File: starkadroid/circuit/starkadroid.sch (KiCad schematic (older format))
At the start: 19 parts, among them IC1 ATMEGA8-P, X1 16MHz

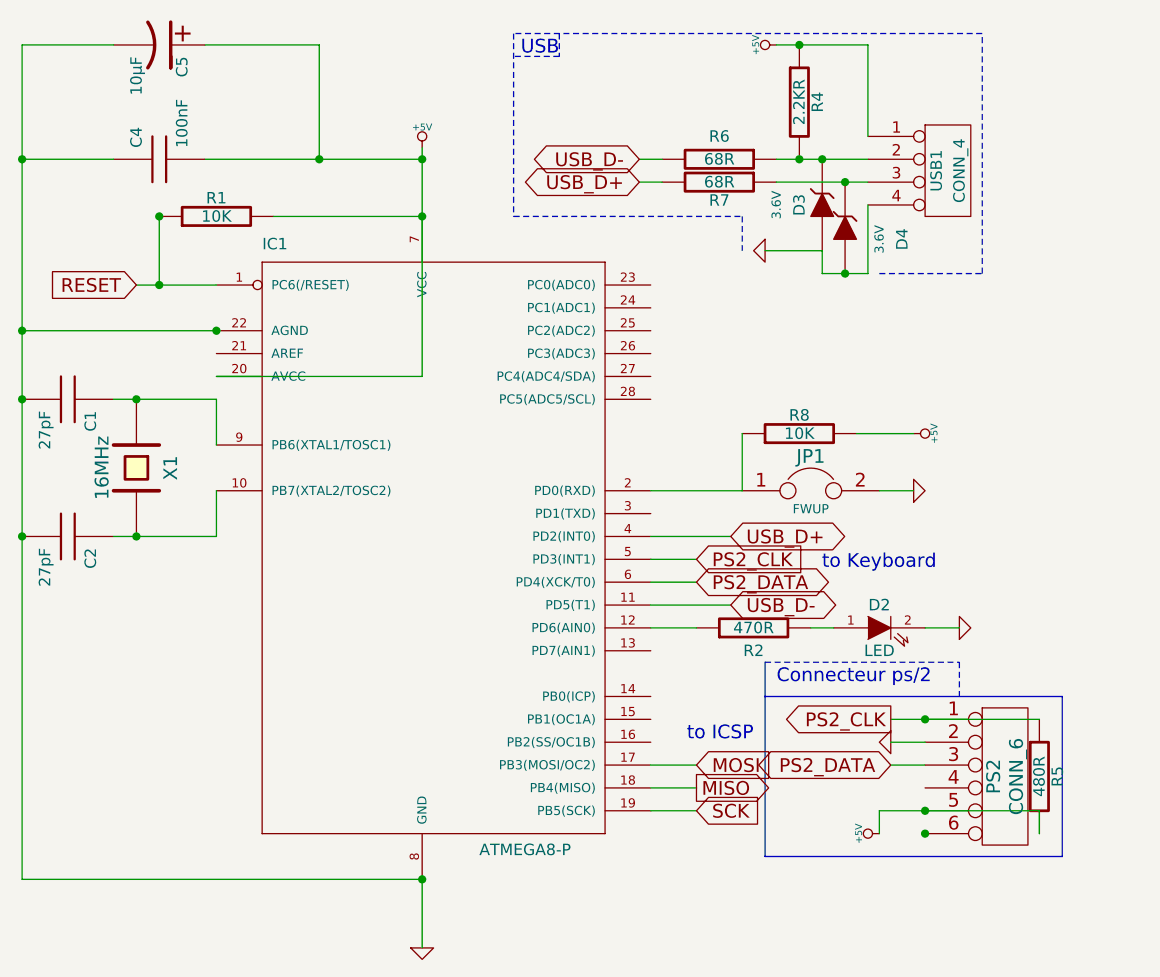
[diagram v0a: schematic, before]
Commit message: Circuit finalisé prêt à être réalisé.
git-svn-id: svn://pulkomandy.tk/avrstuff@24 c6672c3c-f6b6-47f9-9001-1fd6b12fecbe
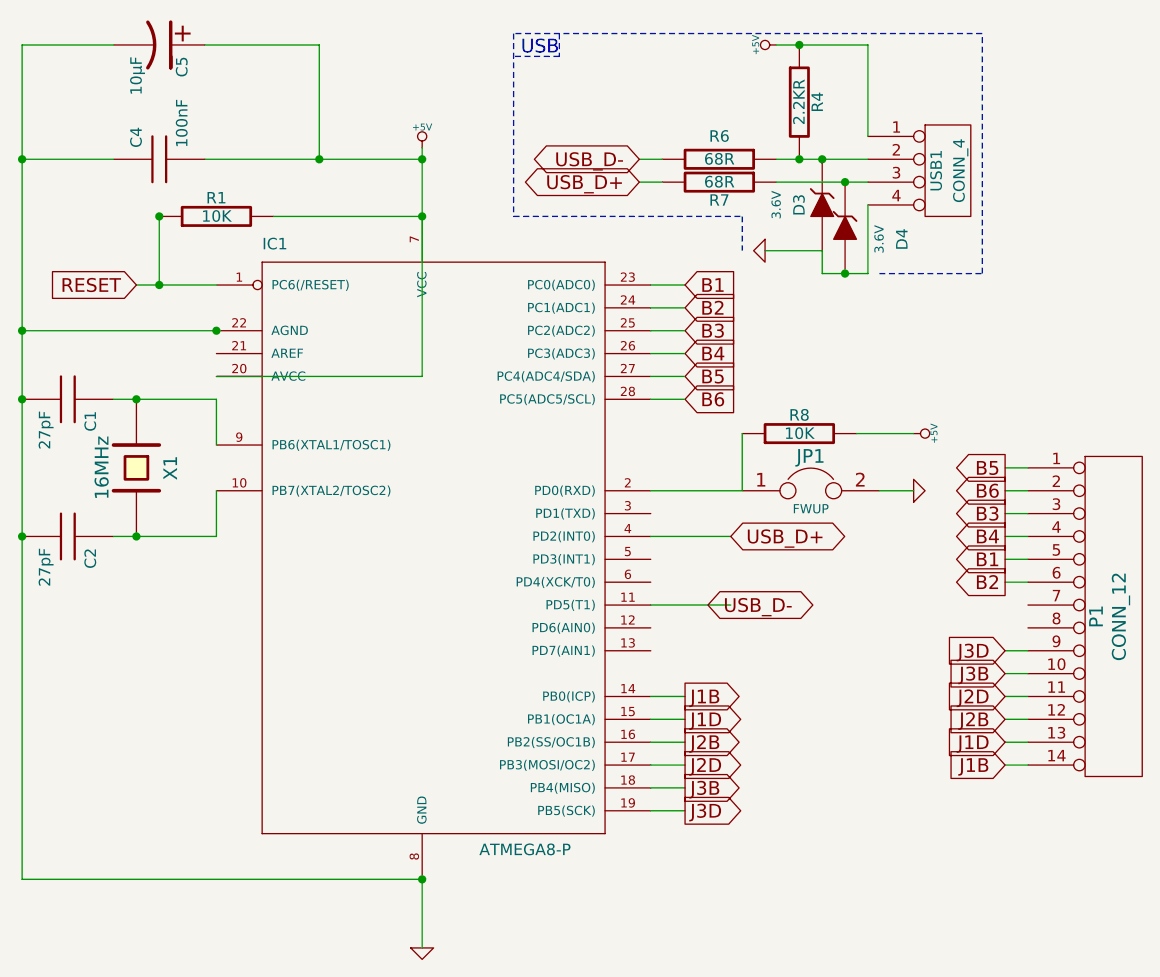
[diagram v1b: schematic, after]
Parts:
- removed D2: LED, symbol LED
- removed PS2: CONN_6, Mini_din6, symbol CONN_6
- removed R2: 470R, symbol R
- removed R5: 480R, symbol R
- added P1: CONN_12, CONN_14, symbol CONN_14
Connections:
- net J1B: now reaches IC1.14 (PB0(ICP))
- net J1B: now also P1.14 (P14)
- net J1D: now reaches IC1.15 (PB1(OC1A))
- net J1D: now also P1.13 (P13)
- net J2B: now reaches IC1.16 (PB2(SS/OC1B))
- net J2B: now also P1.12 (P12)
- net B1: now reaches IC1.23 (PC0(ADC0))
- net B1: now also P1.5 (P5)
- net B2: now reaches IC1.24 (PC1(ADC1))
- net B2: now also P1.6 (P6)
- net B3: now reaches IC1.25 (PC2(ADC2))
- net B3: now also P1.3 (P3)
- net B4: now reaches IC1.26 (PC3(ADC3))
- net B4: now also P1.4 (P4)
- net B5: now reaches IC1.27 (PC4(ADC4/SDA))
- net B5: now also P1.1 (P1)
- net B6: now reaches IC1.28 (PC5(ADC5/SCL))
- net B6: now also P1.2 (P2)
- net MISO renamed J3B
- net J3B: now also P1.10 (P10)
- net MOSI renamed J2D
- net J2D: now also P1.11 (P11)
- net PS2_CLK: no longer names the net of IC1.5 (PD3(INT1))
- net PS2_DATA: no longer names the net of IC1.6 (PD4(XCK/T0))
- net SCK renamed J3D
- net J3D: now also P1.9 (P9)
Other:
- note removed: "Connecteur ps/2"
- note removed: "to ICSP"
- note removed: "to Keyboard"
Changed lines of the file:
@@
-EESchema Schematic File Version 2  date 30/08/2010 19:46:30
+EESchema Schematic File Version 2  date 16/10/2010 15:14:04
 LIBS:power
 LIBS:device
@@
 LIBS:contrib
 LIBS:valves
-LIBS:ps2toserial-cache
+LIBS:starkadroid-cache
 EELAYER 24  0
 EELAYER END
 $Descr User 6000 6000
 Sheet 1 1
-Title "PS/2 to serial converter"
-Date "30 aug 2010"
-Rev "2010.06.22"
+Title "Starkadroid USB Arcade buttons device"
+Date "16 oct 2010"
+Rev "2010.10.16"
 Comp "PulkoTronics"
 Comment1 ""
@@
 Comment4 ""
 $EndDescr
-Connection ~ 4550 4000
-Wire Wire Line
-	5050 4100 5050 4000
-Wire Wire Line
-	5050 4000 4350 4000
+Wire Wire Line
+	4900 3800 5000 3800
+Wire Wire Line
+	4900 3700 5000 3700
+Wire Wire Line
+	4900 3600 5000 3600
+Wire Wire Line
+	4900 3500 5000 3500
+Wire Wire Line
+	4900 3400 5000 3400
+Wire Wire Line
+	4900 3300 5000 3300
+Wire Wire Line
+	3350 4000 3500 4000
+Wire Wire Line
+	3350 3800 3500 3800
+Wire Wire Line
+	3350 3600 3500 3600
+Wire Wire Line
+	4900 2500 5000 2500
+Wire Wire Line
+	4900 2700 5000 2700
+Wire Wire Line
+	4900 3000 5000 3000
+Wire Wire Line
+	3350 2200 3500 2200
+Wire Wire Line
+	3350 2000 3500 2000
+Wire Wire Line
+	3350 1800 3500 1800
 Wire Wire Line
 	4500 2350 4250 2350
 Wire Wire Line
 	3750 2350 3750 2600
-Wire Bus Line
-	3850 3500 5150 3500
-Wire Bus Line
-	5150 3500 5150 4200
-Wire Bus Line
-	5150 4200 3850 4200
-Wire Bus Line
-	3850 4200 3850 3350
-Wire Wire Line
-	4400 3600 5050 3600
-Wire Wire Line
-	1000 650  600  650
+Wire Wire Line
+	600  650  1000 650
 Wire Wire Line
 	600  650  600  4300
-Wire Wire Line
-	4550 3800 4400 3800
 Wire Wire Line
 	3700 3100 3350 3100
@@
 Connection ~ 4200 1650
 Wire Wire Line
-	4300 1350 4300 1650
+	4300 1650 4300 1350
 Wire Wire Line
 	4300 1650 4100 1650
@@
 	3300 1150 3400 1150
 Wire Wire Line
-	4300 1050 4300 650
+	4300 650  4300 1050
 Connection ~ 4100 1150
 Connection ~ 600  1150
@@
 	600  1150 1000 1150
 Wire Wire Line
-	4050 3200 4150 3200
-Wire Wire Line
-	1700 1400 2350 1400
+	2350 1400 1700 1400
 Connection ~ 600  1900
 Wire Wire Line
 	1100 1700 1450 1700
-Wire Wire Line
-	3350 4000 3550 4000
-Wire Wire Line
-	3350 3800 3550 3800
 Wire Wire Line
 	600  1900 1450 1900
@@
 	1000 2200 1450 2200
 Wire Wire Line
-	1450 2600 1450 2800
+	1450 2800 1450 2600
 Connection ~ 2350 4300
-Wire Notes Line
-	3850 3350 4700 3350
-Wire Wire Line
-	3350 2900 3550 2900
-Wire Wire Line
-	3350 3000 3550 3000
-Wire Notes Line
-	4700 3350 4700 3500
-Wire Wire Line
-	1450 2100 2350 2100
-Wire Wire Line
-	2350 2100 2350 1100
+Wire Wire Line
+	2350 2100 1450 2100
+Wire Wire Line
+	2350 1100 2350 2100
 Connection ~ 2350 1400
 Wire Wire Line
 	1450 2200 1450 2400
 Wire Wire Line
-	1450 2800 1000 2800
+	1000 2800 1450 2800
 Connection ~ 1100 2800
 Connection ~ 1450 1900
@@
 	2350 4300 600  4300
 Connection ~ 600  2800
-Wire Wire Line
-	3350 3900 3550 3900
 Connection ~ 1200 1700
 Connection ~ 2350 1150
 Connection ~ 1200 1400
 Wire Wire Line
-	3350 3200 3550 3200
-Wire Wire Line
-	4550 3200 4700 3200
-Wire Wire Line
 	1400 1150 2350 1150
 Connection ~ 1900 1150
@@
 Connection ~ 4200 1250
 Wire Wire Line
-	4300 650  3900 650
+	3900 650  4300 650
 Connection ~ 4000 650
 Wire Wire Line
@@
 	3700 2800 3350 2800
 Wire Wire Line
-	4550 3700 4400 3700
-Wire Wire Line
 	1200 1400 1200 1700
 Wire Wire Line
@@
 Wire Wire Line
 	1900 650  1900 1150
-Connection ~ 4550 3600
-Connection ~ 4550 4100
 Wire Wire Line
 	3750 2600 3350 2600
@@
 	4350 2600 4500 2600
 Wire Wire Line
-	4350 4000 4350 4100
+	3350 1700 3500 1700
+Wire Wire Line
+	3350 1900 3500 1900
+Wire Wire Line
+	3350 2100 3500 2100
+Wire Wire Line
+	4900 2900 5000 2900
+Wire Wire Line
+	4900 2800 5000 2800
+Wire Wire Line
+	4900 2600 5000 2600
+Wire Wire Line
+	3350 3500 3500 3500
+Wire Wire Line
+	3350 3700 3500 3700
+Wire Wire Line
+	3350 3900 3500 3900
+Text GLabel 4900 3300 0    60   Input ~ 0
+J3D
+Text GLabel 4900 3400 0    60   Input ~ 0
+J3B
+Text GLabel 4900 3500 0    60   Input ~ 0
+J2D
+Text GLabel 4900 3600 0    60   Input ~ 0
+J2B
+Text GLabel 4900 3700 0    60   Input ~ 0
+J1D
+Text GLabel 4900 3800 0    60   Input ~ 0
+J1B
+Text GLabel 3500 4000 2    60   Output ~ 0
+J3D
+Text GLabel 3500 3900 2    60   Output ~ 0
+J3B
+Text GLabel 3500 3700 2    60   Output ~ 0
+J2B
+Text GLabel 3500 3800 2    60   Output ~ 0
+J2D
+Text GLabel 3500 3600 2    60   Output ~ 0
+J1D
+Text GLabel 3500 3500 2    60   Output ~ 0
+J1B
+Text GLabel 4900 2600 0    60   Output ~ 0
+B6
+Text GLabel 4900 2500 0    60   Output ~ 0
+B5
+Text GLabel 4900 2800 0    60   Output ~ 0
+B4
+Text GLabel 4900 2700 0    60   Output ~ 0
+B3
+Text GLabel 4900 3000 0    60   Output ~ 0
+B2
+Text GLabel 4900 2900 0    60   Output ~ 0
+B1
+Text GLabel 3500 2200 2    60   Input ~ 0
+B6
+Text GLabel 3500 2100 2    60   Input ~ 0
+B5
+Text GLabel 3500 2000 2    60   Input ~ 0
+B4
+Text GLabel 3500 1900 2    60   Input ~ 0
+B3
+Text GLabel 3500 1800 2    60   Input ~ 0
+B2
+Text GLabel 3500 1700 2    60   Input ~ 0
+B1
+$Comp
+L CONN_14 P1
+U 1 1 4CB98E65
+P 5350 3150
+F 0 "P1" V 5300 3150 60  0000 C CNN
+F 1 "CONN_12" V 5400 3150 60  0000 C CNN
+F 2 "CONN_14" V 5240 3090 60  0001 C CNN
+	1    5350 3150
+	1    0    0    -1
+$EndComp
 $Comp
 L JUMPER JP1
@@
 	1    0    0    -1
 $EndComp
-Text GLabel 3700 3100 2    60   BiDi ~ 0
+Text GLabel 3600 3100 2    60   BiDi ~ 0
 USB_D-
 Text GLabel 3700 2800 2    60   BiDi ~ 0
 USB_D+
-$Comp
-L R R5
-U 1 1 4C21EEDC
-P 5050 3850
-F 0 "R5" V 5130 3850 50  0000 C CNN
-F 1 "480R" V 5050 3850 50  0000 C CNN
-	1    5050 3850
-	1    0    0    -1
-$EndComp
-Text Notes 3800 3700 2    60   ~ 0
-to ICSP
-Text Notes 4600 2950 2    60   ~ 0
-to Keyboard
 $Comp
 L C C4
@@
 $EndComp
 $Comp
-L GND #PWR05
-U 1 1 4C20B3CD
-P 4700 3200
-F 0 "#PWR05" H 4700 3200 30  0001 C CNN
-F 1 "GND" H 4700 3130 30  0001 C CNN
-	1    4700 3200
-	0    -1   -1   0
-$EndComp
-$Comp
-L LED D2
-U 1 1 4C20B393
-P 4350 3200
-F 0 "D2" H 4350 3300 50  0000 C CNN
-F 1 "LED" H 4350 3100 50  0000 C CNN
-	1    4350 3200
-	1    0    0    -1
-$EndComp
-$Comp
-L R R2
-U 1 1 4C20B383
-P 3800 3200
-F 0 "R2" V 3700 3200 50  0000 C CNN
-F 1 "470R" V 3800 3200 50  0000 C CNN
-	1    3800 3200
-	0    -1   -1   0
-$EndComp
-$Comp
 L R R1
 U 1 1 4C20B267
@@
 	0    -1   -1   0
 $EndComp
-Text GLabel 3550 4000 2    60   Input ~ 0
-SCK
 Text GLabel 1100 1700 0    60   Input ~ 0
 RESET
-Text GLabel 3550 3900 2    60   Output ~ 0
-MISO
-Text GLabel 3550 3800 2    60   Input ~ 0
-MOSI
 $Comp
 L C C2
@@
 $EndComp
 $Comp
-L +5V #PWR06
-U 1 1 4C20ABFF
-P 4350 4100
-F 0 "#PWR06" H 4350 4190 20  0001 C CNN
-F 1 "+5V" H 4350 4190 30  0000 C CNN
-	1    4350 4100
-	0    -1   -1   0
-$EndComp
-$Comp
-L GND #PWR07
-U 1 1 4C20ABF2
-P 4400 3700
-F 0 "#PWR07" H 4400 3700 30  0001 C CNN
-F 1 "GND" H 4400 3630 30  0001 C CNN
-	1    4400 3700
-	0    1    1    0
-$EndComp
-Text Notes 3900 3450 0    60   ~ 0
-Connecteur ps/2
-Text GLabel 3550 3000 2    60   BiDi ~ 0
-PS2_DATA
-Text GLabel 4400 3800 0    60   BiDi ~ 0
-PS2_DATA
-Text GLabel 4400 3600 0    60   Output ~ 0
-PS2_CLK
-Text GLabel 3550 2900 2    60   Input ~ 0
-PS2_CLK
-$Comp
-L GND #PWR08
+L GND #PWR05
 U 1 1 4C20AAB2
 P 2350 4600
-F 0 "#PWR08" H 2350 4600 30  0001 C CNN
+F 0 "#PWR05" H 2350 4600 30  0001 C CNN
 F 1 "GND" H 2350 4530 30  0001 C CNN
 	1    2350 4600
@@
 $EndComp
 $Comp
-L +5V #PWR09
+L +5V #PWR06
 U 1 1 4C20AAA4
 P 2350 1100
-F 0 "#PWR09" H 2350 1190 20  0001 C CNN
+F 0 "#PWR06" H 2350 1190 20  0001 C CNN
 F 1 "+5V" H 2350 1190 30  0000 C CNN
 	1    2350 1100
 	1    0    0    -1
 $EndComp
-$Comp
-L CONN_6 PS2
-U 1 1 4C20A3B4
-P 4900 3850
-F 0 "PS2" V 4850 3850 60  0000 C CNN
-F 1 "CONN_6" V 4950 3850 60  0000 C CNN
-F 2 "Mini_din6" V 4790 3790 60  0001 C CNN
-	1    4900 3850
-	1    0    0    -1
-$EndComp

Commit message: * Ajout de pins "extra" sur le PCB. On sait jamais ça peut toujours servir...  * Gros nettoyage du code qui est maintenant fonctionnel.
git-svn-id: svn://pulkomandy.tk/avrstuff@25 c6672c3c-f6b6-47f9-9001-1fd6b12fecbe
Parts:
- added P2, P3, P4, P5, P6: CONN_1, symbol CONN_1
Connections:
- net at IC1.12 (PD6(AIN0)): now also P5.1
- net at IC1.13 (PD7(AIN1)): now also P6.1
- net at IC1.3 (PD1(TXD)): now also P2.1
- net at IC1.5 (PD3(INT1)): now also P3.1
- net at IC1.6 (PD4(XCK/T0)): now also P4.1
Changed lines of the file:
@@
-EESchema Schematic File Version 2  date 16/10/2010 15:14:04
+EESchema Schematic File Version 2  date 17/10/2010 21:54:16
 LIBS:power
 LIBS:device
@@
 Sheet 1 1
 Title "Starkadroid USB Arcade buttons device"
-Date "16 oct 2010"
+Date "17 oct 2010"
 Rev "2010.10.16"
 Comp "PulkoTronics"
@@
 Comment4 ""
 $EndDescr
+$Comp
+L CONN_1 P?
+U 1 1 4CBB4DB2
+P 3550 3300
+AR Path="/4CBB4DAA" Ref="P?"  Part="1"
+AR Path="/4CBB4DB2" Ref="P6"  Part="1"
+F 0 "P6" H 3630 3300 40  0000 L CNN
+F 1 "CONN_1" H 3550 3355 30  0001 C CNN
+	1    3550 3300
+	1    0    0    -1
+$EndComp
+$Comp
+L CONN_1 P?
+U 1 1 4CBB4DB1
+P 3550 3200
+AR Path="/4CBB4DAA" Ref="P?"  Part="1"
+AR Path="/4CBB4DB1" Ref="P5"  Part="1"
+F 0 "P5" H 3630 3200 40  0000 L CNN
+F 1 "CONN_1" H 3550 3255 30  0001 C CNN
+	1    3550 3200
+	1    0    0    -1
+$EndComp
+$Comp
+L CONN_1 P?
+U 1 1 4CBB4DAE
+P 3550 3000
+AR Path="/4CBB4DAA" Ref="P?"  Part="1"
+AR Path="/4CBB4DAE" Ref="P4"  Part="1"
+F 0 "P4" H 3630 3000 40  0000 L CNN
+F 1 "CONN_1" H 3550 3055 30  0001 C CNN
+	1    3550 3000
+	1    0    0    -1
+$EndComp
+$Comp
+L CONN_1 P3
+U 1 1 4CBB4DAA
+P 3550 2900
+F 0 "P3" H 3630 2900 40  0000 L CNN
+F 1 "CONN_1" H 3550 2955 30  0001 C CNN
+	1    3550 2900
+	1    0    0    -1
+$EndComp
+$Comp
+L CONN_1 P2
+U 1 1 4CBB4DA3
+P 3550 2700
+F 0 "P2" H 3630 2700 40  0000 L CNN
+F 1 "CONN_1" H 3550 2755 30  0001 C CNN
+	1    3550 2700
+	1    0    0    -1
+$EndComp
+Wire Wire Line
+	3350 3300 3400 3300
+Wire Wire Line
+	3400 3000 3350 3000
+Wire Wire Line
+	3350 2900 3400 2900
 Wire Wire Line
 	4900 3800 5000 3800
@@
 	3750 2350 3750 2600
 Wire Wire Line
-	600  650  1000 650
+	1000 650  600  650
 Wire Wire Line
 	600  650  600  4300
@@
 Connection ~ 4200 1650
 Wire Wire Line
-	4300 1650 4300 1350
+	4300 1350 4300 1650
 Wire Wire Line
 	4300 1650 4100 1650
@@
 	3300 1150 3400 1150
 Wire Wire Line
-	4300 650  4300 1050
+	4300 1050 4300 650
 Connection ~ 4100 1150
 Connection ~ 600  1150
@@
 	1000 2200 1450 2200
 Wire Wire Line
-	1450 2800 1450 2600
+	1450 2600 1450 2800
 Connection ~ 2350 4300
 Wire Wire Line
-	2350 2100 1450 2100
-Wire Wire Line
-	2350 1100 2350 2100
+	1450 2100 2350 2100
+Wire Wire Line
+	2350 2100 2350 1100
 Connection ~ 2350 1400
 Wire Wire Line
 	1450 2200 1450 2400
 Wire Wire Line
-	1000 2800 1450 2800
+	1450 2800 1000 2800
 Connection ~ 1100 2800
 Connection ~ 1450 1900
@@
 Connection ~ 4200 1250
 Wire Wire Line
-	3900 650  4300 650
+	4300 650  3900 650
 Connection ~ 4000 650
 Wire Wire Line
@@
 Wire Wire Line
 	3350 3900 3500 3900
+Wire Wire Line
+	3350 2700 3400 2700
+Wire Wire Line
+	3350 3200 3400 3200
 Text GLabel 4900 3300 0    60   Input ~ 0
 J3D
